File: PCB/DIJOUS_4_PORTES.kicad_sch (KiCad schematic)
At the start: 0 parts

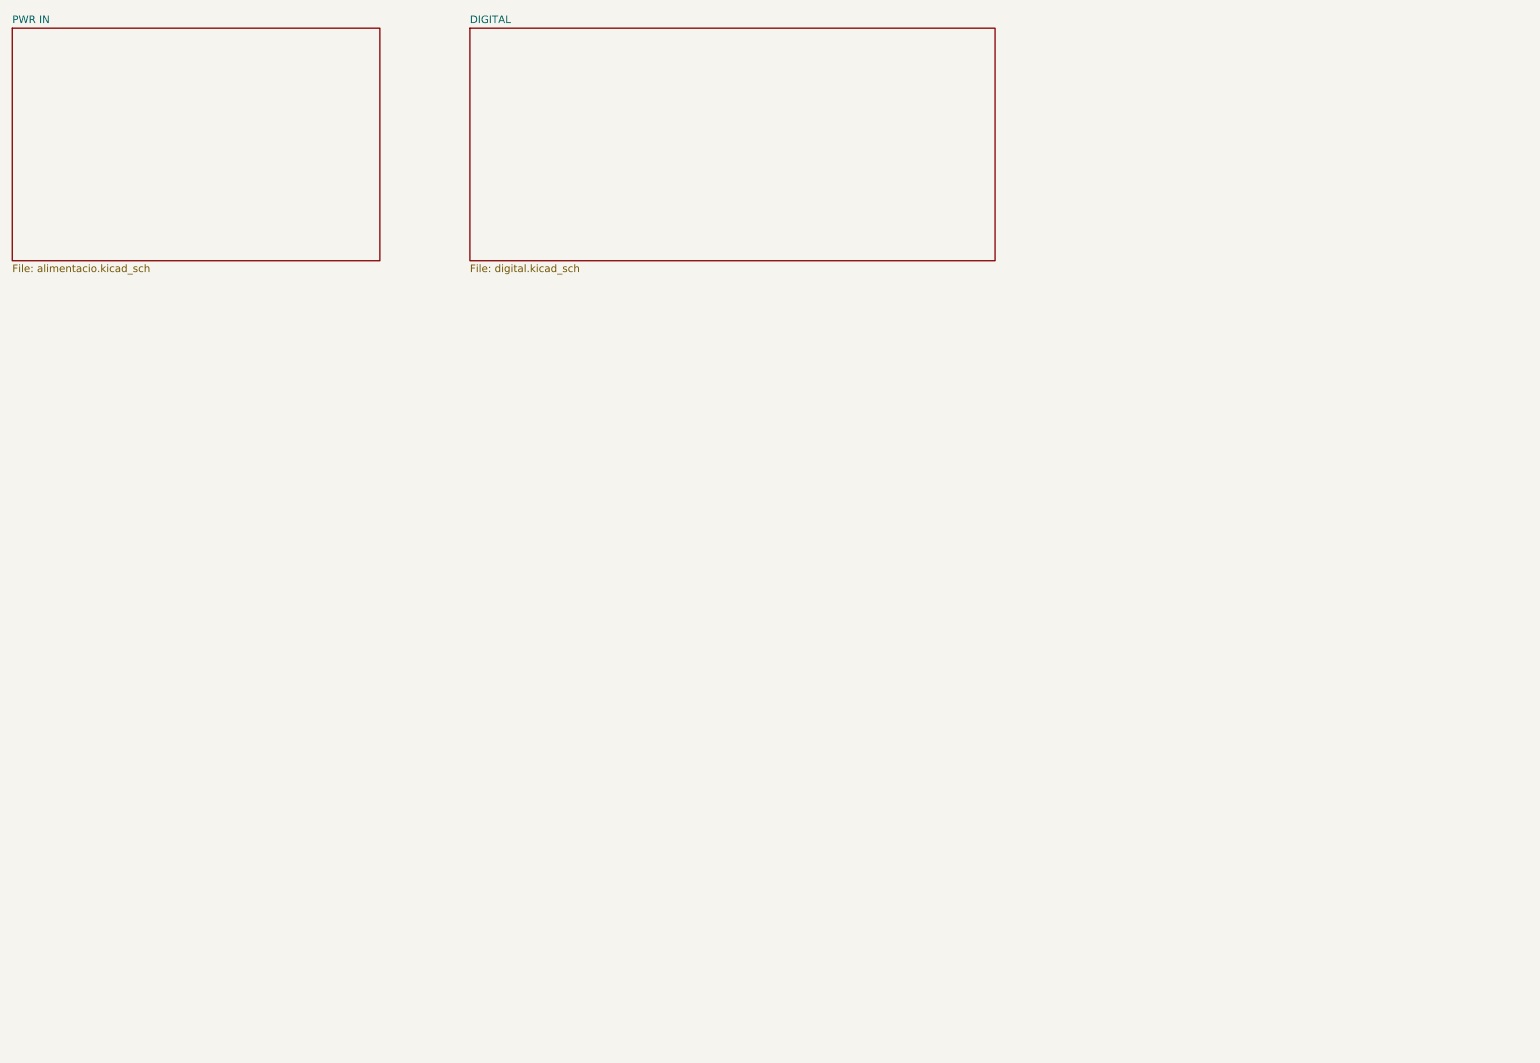
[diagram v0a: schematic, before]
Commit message: falta RFID i final de carrera
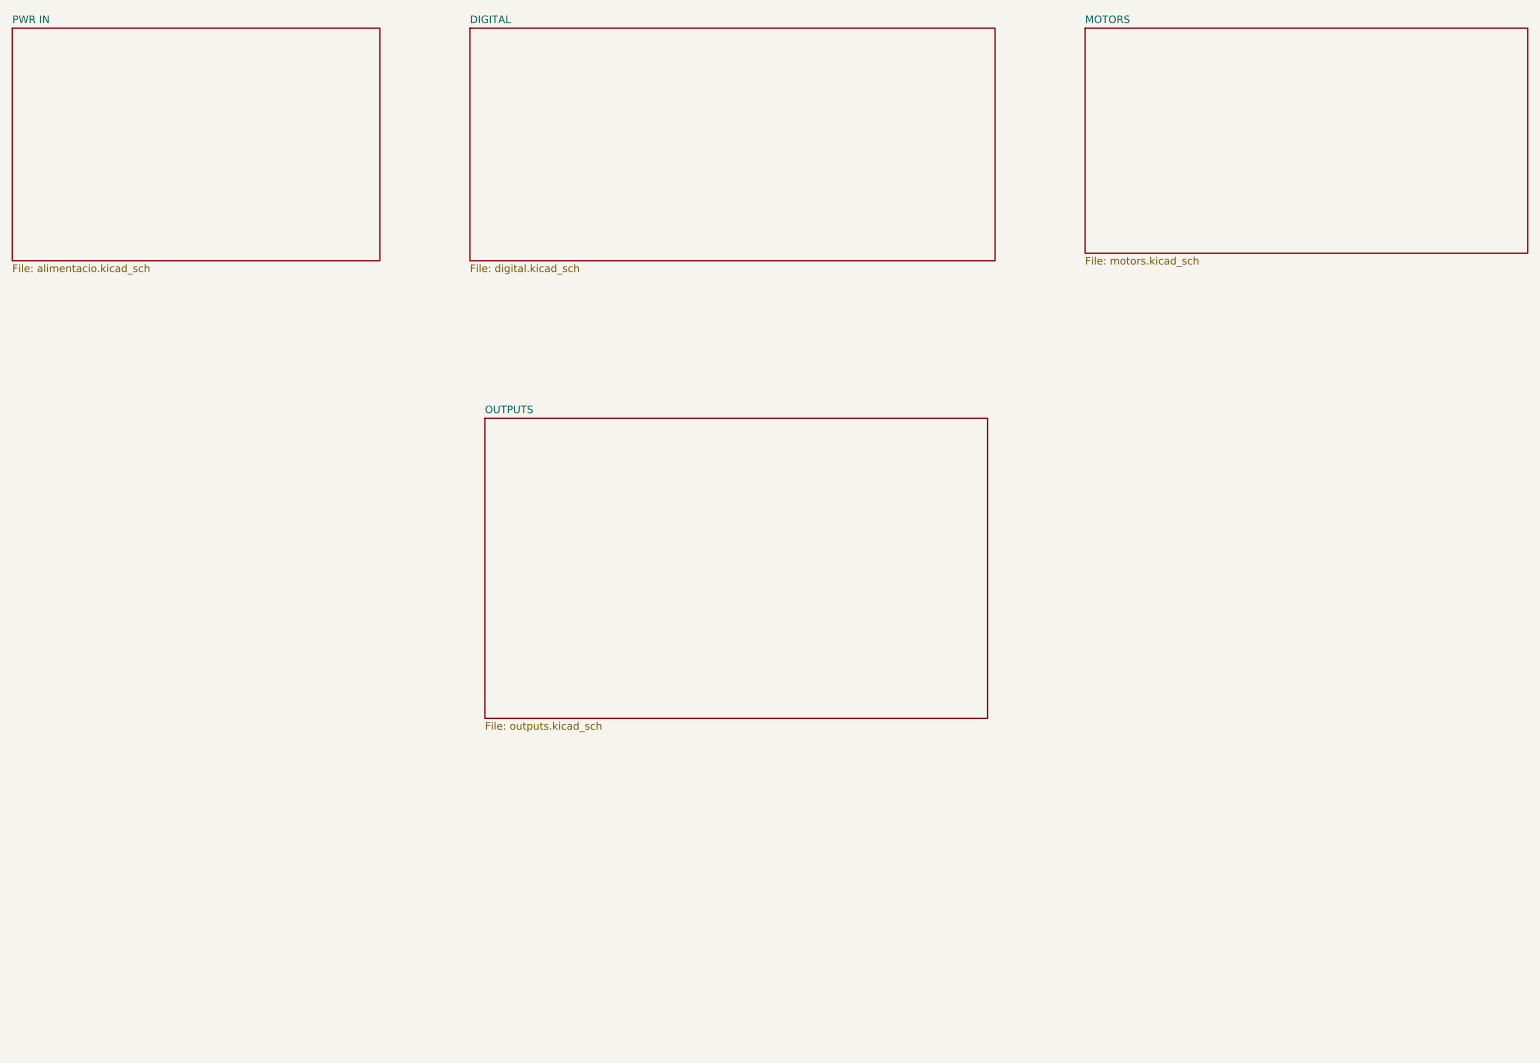
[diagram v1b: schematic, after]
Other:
- added sheet MOTORS (motors.kicad_sch)
- added sheet OUTPUTS (outputs.kicad_sch)
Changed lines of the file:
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@@
+    )
+  )
+  (sheet (at 201.93 21.59) (size 74.93 38.1) (fields_autoplaced)
+    (stroke (width 0.1524) (type solid))
+    (fill (color 0 0 0 0.0000))
+    (property "Sheetname" "MOTORS" (at 201.93 20.8784 0)
+      (effects (font (size 1.27 1.27)) (justify left bottom))
+    )
+    (property "Sheetfile" "motors.kicad_sch" (at 201.93 60.2746 0)
+      (effects (font (size 1.27 1.27)) (justify left top))
+    )
+    (property "Campo2" "" (at 201.93 21.59 0)
+      (effects (font (size 1.27 1.27)) hide)
+    )
+    (instances
+      (project "DIJOUS_4_PORTES"
+        (path "/69b34976-047e-478e-bd76-9b6ef0dba356" (page "4"))
+      )
     )
   )
@@
       )
     )
+  )
+  (sheet (at 100.33 87.63) (size 85.09 50.8) (fields_autoplaced)
+    (stroke (width 0.1524) (type solid))
+    (fill (color 0 0 0 0.0000))
+    (property "Sheetname" "OUTPUTS" (at 100.33 86.9184 0)
+      (effects (font (size 1.27 1.27)) (justify left bottom))
+    )
+    (property "Sheetfile" "outputs.kicad_sch" (at 100.33 139.0146 0)
+      (effects (font (size 1.27 1.27)) (justify left top))
+    )
+    (property "Campo2" "" (at 100.33 87.63 0)
+      (effects (font (size 1.27 1.27)) hide)
+    )
+    (instances
+      (project "DIJOUS_4_PORTES"
+        (path "/69b34976-047e-478e-bd76-9b6ef0dba356" (page "5"))
+      )
+    )

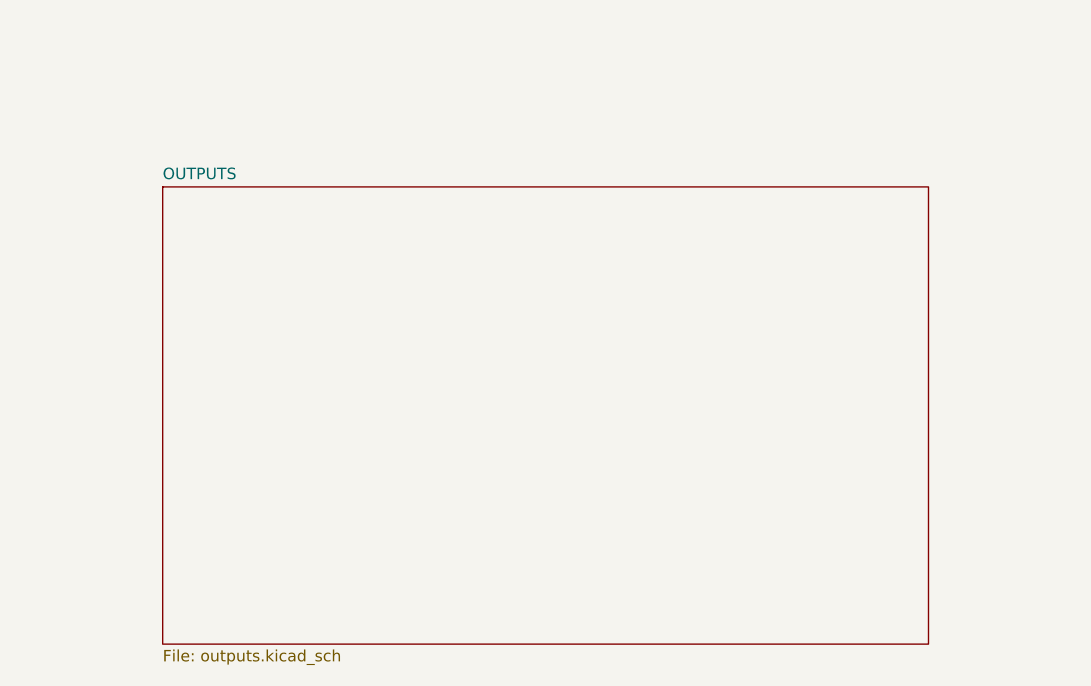
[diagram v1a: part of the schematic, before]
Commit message: change file structure
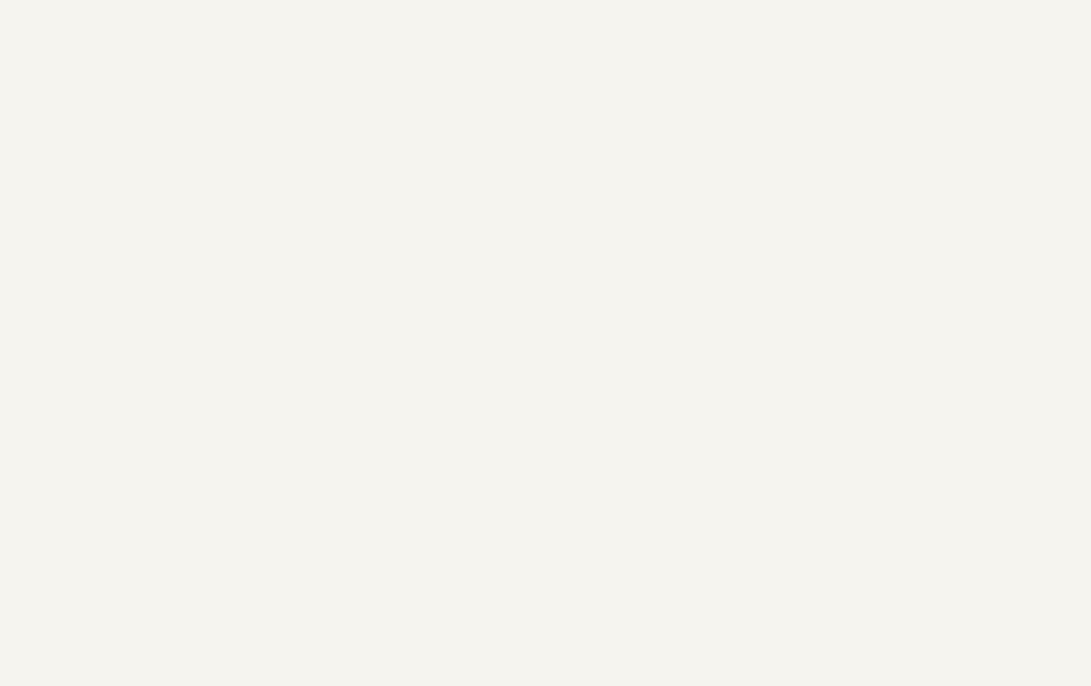
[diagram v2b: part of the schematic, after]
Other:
- removed sheet OUTPUTS
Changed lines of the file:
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@@
-    )
-  )
-  (sheet (at 100.33 87.63) (size 85.09 50.8) (fields_autoplaced)
-    (stroke (width 0.1524) (type solid))
-    (fill (color 0 0 0 0.0000))
-    (property "Sheetname" "OUTPUTS" (at 100.33 86.9184 0)
-      (effects (font (size 1.27 1.27)) (justify left bottom))
-    )
-    (property "Sheetfile" "outputs.kicad_sch" (at 100.33 139.0146 0)
-      (effects (font (size 1.27 1.27)) (justify left top))
-    )
-    (property "Campo2" "" (at 100.33 87.63 0)
-      (effects (font (size 1.27 1.27)) hide)
-    )
-    (instances
-      (project "DIJOUS_4_PORTES"
-        (path "/69b34976-047e-478e-bd76-9b6ef0dba356" (page "5"))
-      )
     )
   )

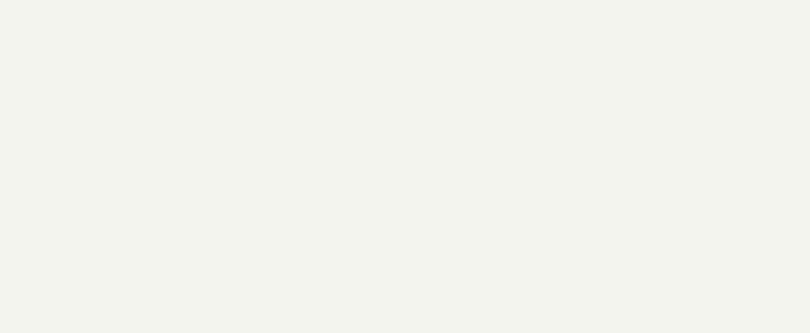
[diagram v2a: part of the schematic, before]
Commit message: first PCB done, need to correct vias and solve all DRC errors
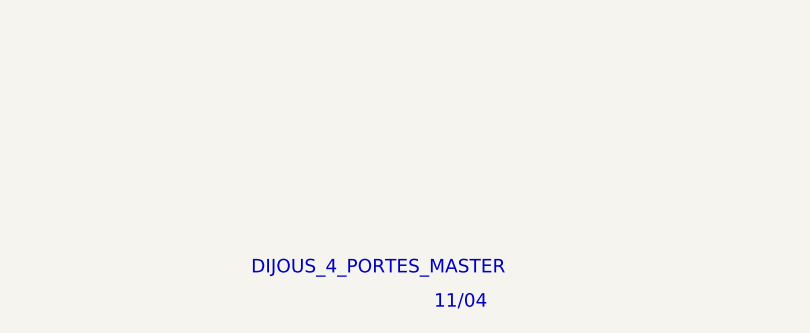
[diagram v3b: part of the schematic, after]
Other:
- note added: "11/04"
- note added: "DIJOUS_4_PORTES_MASTER"
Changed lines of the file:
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@@
 (kicad_sch (version 20230121) (generator eeschema)
   (paper "A4")
+  (text "11/04" (at 207.01 194.31 0)
+    (effects (font (size 1.5 1.5)) (justify left bottom))
+  )
+  (text "DIJOUS_4_PORTES_MASTER" (at 186.69 190.5 0)
+    (effects (font (size 1.5 1.5)) (justify left bottom))
+  )
   (sheet (at 20.32 21.59) (size 62.23 39.37) (fields_autoplaced)
     (stroke (width 0.1524) (type solid))
